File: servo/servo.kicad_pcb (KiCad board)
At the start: 2 copper layers, 20.2 x 18.2 mm, 10 parts, among them J1 Servo 1, J2 Servo 2, J3 System, J4 I/O, U1 STM32F030K6Tx

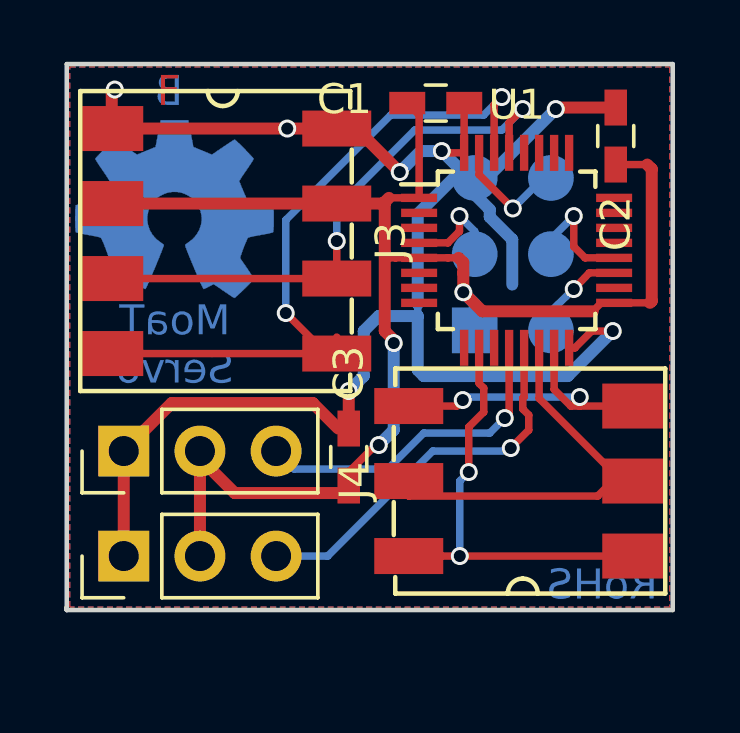
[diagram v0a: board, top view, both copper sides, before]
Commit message: servo update
?
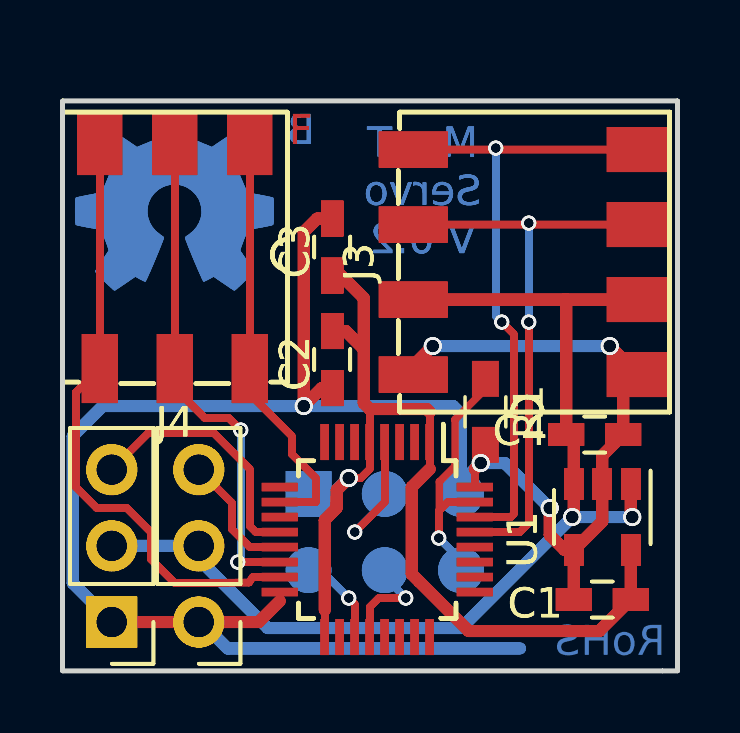
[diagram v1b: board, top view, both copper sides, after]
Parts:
- added C1: 1µF, Capacitors_SMD:C_0603_HandSoldering, F.Cu at (161.4, 114.0)
- added C2: 10nF, Capacitors_SMD:C_0603_HandSoldering, F.Cu at (152.4, 106.0)
- added C3: 100nF, Capacitors_SMD:C_0603_HandSoldering, F.Cu at (152.4, 102.2)
- added C4 (x2): 1µF, Capacitors_SMD:C_0603_HandSoldering, F.Cu at (161.2, 108.5)
- added J1: Servo 1, Pin_Headers:Pin_Header_Straight_1x03_Pitch2.54mm, F.Cu at (145.1, 114.7)
- added J2: Servo 2, Pin_Headers:Pin_Header_Straight_1x03_Pitch2.54mm, F.Cu at (148.0, 114.7)
- added J3: System, MoaT:AVX_9276_4Pin_HS, F.Cu at (158.9, 102.7)
- added J4: I/O, MoaT:AVX_9276_3Pin_HS, F.Cu at (147.2, 102.5)
- added OSHW: OSHW-Symbol_6.7x6mm_Copper, Symbols:OSHW-Symbol_6.7x6mm_Copper, B.Cu at (147.2, 100.7)
- added Prog1: PogoPad, MoaT:PogoPad_2x3_SMD, B.Cu at (154.2, 111.7)
- added R1: 10k, Resistors_SMD:R_0603_HandSoldering, F.Cu at (157.6, 107.7)
- added U1: STM32F030K6Tx, Housings_QFP:LQFP-32_5x5mm_Pitch0.5mm, F.Cu at (153.9, 112.0)
- added U2 (x2): TPS76333, TO_SOT_Packages_SMD:SOT-23-5, F.Cu at (161.4, 111.2)
- moved C1 17.5 mm to (161.4, 114.0), turned to 180 degrees
- moved J4 13.8 mm to (147.2, 102.5), turned to 180 degrees
- moved C2 12.0 mm to (152.4, 106.0), turned to 270 degrees
- moved U1 10.7 mm to (153.9, 112.0), turned to 270 degrees
- moved Prog1 10.2 mm to (154.2, 111.7), turned to 270 degrees
- moved J3 10.2 mm to (158.9, 102.7), turned to 90 degrees
- moved C3 7.02 mm to (152.4, 102.2)
- moved J1 5.71 mm to (145.1, 114.7), turned to 180 degrees
- moved J2 3.33 mm to (148.0, 114.7), turned to 180 degrees
- moved OSHW 0.25 mm to (147.2, 100.7)
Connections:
- net Net-(J1-Pad3) renamed /Servo1
- net Net-(J2-Pad3) renamed /Servo2
- J1 pad 2: +3V3 -> +5V
- J2 pad 2: +3V3 -> +5V
- J3 pad 2: +3V3 -> +5V
- U1 pad 11: Net-(U1-Pad11) -> (no net)
- U1 pad 18: Net-(U1-Pad18) -> (no net)
- U1 pad 2: Net-(U1-Pad2) -> (no net)
- U1 pad 21: Net-(U1-Pad21) -> (no net)
- U1 pad 22: Net-(U1-Pad22) -> (no net)
- U1 pad 23: Net-(U1-Pad23) -> (no net)
- U1 pad 24: Net-(U1-Pad24) -> (no net)
- U1 pad 25: Net-(U1-Pad25) -> (no net)
- U1 pad 26: Net-(U1-Pad26) -> (no net)
- U1 pad 27: Net-(U1-Pad27) -> (no net)
- U1 pad 28: Net-(U1-Pad28) -> (no net)
- U1 pad 3: Net-(U1-Pad3) -> (no net)
- U1 pad 6: Net-(U1-Pad6) -> (no net)
- U1 pad 7: Net-(U1-Pad7) -> (no net)
- U1 pad 8: Net-(U1-Pad8) -> (no net)
- U1 pad 9: Net-(U1-Pad9) -> (no net)
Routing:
- net GND: track 61.7 -> 146.0 mm, vias 7 -> 10
- net +5V: track 0.00 -> 72.6 mm, vias 0 -> 4
- net Net-(J4-Pad3): track 10.4 -> 41.1 mm, vias 2 -> 0
- net /SCL: track 19.3 -> 39.1 mm, vias 2 -> 4
- net Net-(J4-Pad2): track 14.4 -> 33.5 mm, vias 0 -> 4
- net /SDA: track 24.3 -> 42.9 mm, vias 2 -> 4
- net +3V3: track 51.4 -> 68.6 mm, vias 3 -> 2
- net Net-(J4-Pad1): track 16.0 -> 28.1 mm, vias 2 -> 0
- net Net-(Prog1-Pad6): track 4.01 -> 12.2 mm, vias 1 -> 2
- net Net-(Prog1-Pad3): track 3.49 -> 10.2 mm, vias 1 -> 2
- net /Servo1: track 11.7 -> 17.2 mm, vias 1 -> 0
- net /Servo2: track 13.0 -> 8.57 mm, vias 1 -> 0
- net /Rx: track 4.10 -> 7.09 mm, vias 1 -> 2
- net /Tx: track 3.27 -> 6.22 mm, vias 1 -> 2
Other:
- board size 20.2 x 18.2 mm -> 20.5 x 19 mm
- net class Default: via_dia 0.6 -> 0.5; via_drill 0.4 -> 0.3
- board text added: "MoaT Servo V 0.2"
- board text removed: "MoaT Servo"

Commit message: servo PCB repaired
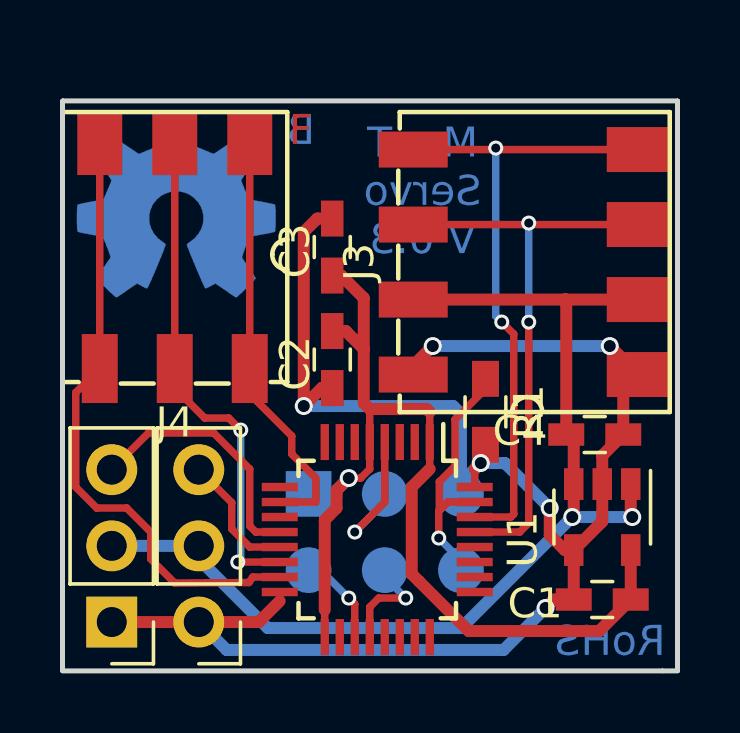
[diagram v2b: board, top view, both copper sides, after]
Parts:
- removed the C1 at (161.4, 114.0)
- removed the C2 at (152.4, 106.0)
- removed the C3 at (152.4, 102.2)
- removed the C4 at (161.2, 108.5)
- removed the J1 at (145.1, 114.7)
- removed the J2 at (148.0, 114.7)
- removed the J3 at (158.9, 102.7)
- removed the J4 at (147.2, 102.5)
- removed OSHW (x2): OSHW-Symbol_6.7x6mm_Copper, Symbols:OSHW-Symbol_6.7x6mm_Copper
- removed the Prog1 at (154.2, 111.7)
- removed the U1 at (153.9, 112.0)
- removed the U2 at (161.4, 111.2)
- added REF***: OSHW-Symbol_6.7x6mm_Copper, Symbols:OSHW-Symbol_6.7x6mm_Copper, B.Cu at (147.3, 100.9)
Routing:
- net GND: track 146.0 -> 61.1 mm, vias 10 -> 6
- net +5V: track 72.6 -> 36.3 mm, vias 4 -> 2
- net +3V3: track 68.6 -> 34.3 mm, vias 2 -> 1
- net /SDA: track 42.9 -> 21.2 mm, vias 4 -> 2
- net Net-(J4-Pad3): track 41.1 -> 20.5 mm
- net /SCL: track 39.1 -> 19.4 mm, vias 4 -> 2
- net Net-(J4-Pad2): track 33.5 -> 16.8 mm, vias 4 -> 2
- net Net-(J4-Pad1): track 28.1 -> 14.1 mm
- net /Servo1: track 17.2 -> 8.59 mm
- net Net-(Prog1-Pad3): track 10.2 -> 5.10 mm, vias 2 -> 1
- net /Servo2: track 8.57 -> 4.28 mm
- net /Rx: track 7.09 -> 3.54 mm, vias 2 -> 1
- net Net-(Prog1-Pad6): track 12.2 -> 9.05 mm, vias 2 -> 1
- net /Tx: track 6.22 -> 3.11 mm, vias 2 -> 1
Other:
- board text added: "MoaT Servo V 0.3"
- board text removed: "MoaT Servo V 0.2"
